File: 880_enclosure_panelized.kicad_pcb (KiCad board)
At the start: 2 copper layers, 351.5 x 39 mm, 182 parts, among them CON1 BARREL_JACK, J1 RUN/STOP, J10 RS IN, J11 CP IN, J12 MA IN, J13 CB IN, J14 CY IN, J15 OH IN, J16 CH IN, J17 IN 1, J18 IN 2, J19 IN 3, J2 SYNC24 CLK, J20 IN 4, J21 MULT IN, J22 SUM, J23 JACK_STEREO, J24 JACK_TRS_SWITCHED, J25 JACK_STEREO, J3 ASSIGN 1, J4 ASSIGN 2, J5 BD IN, J6 SD IN, J7 LT IN, J8 MT IN, J9 HT IN, P1 CONN_02X03, P10 CONN_01X02, P11 CONN_01X03, P2 CONN_01X02, P3 CONN_02X08, P4 CONN_01X03, P5 CONN_01X04, P6 CONN_01X04, P7 CONN_01X03, P8 CONN_01X03, P9 CONN_01X03, Q1 MMBT3904, Q10 MMBT3904, Q11 MMBT3904, Q12 MMBT3904, Q13 MMBT3904, Q14 C945, Q15 A733, Q2 MMBT3904, Q3 MMBT3904, Q4 MMBT3904, Q5 MMBT3904, Q6 MMBT3904, Q7 MMBT3904, Q8 MMBT3904, Q9 MMBT3904, SW1 SPST, U1 74HC165, U2 74HC165, U3 VX078-500, U4 VX078-500, U5 4558, U6 4558, X1 MIDI OUT, X2 SYNC24

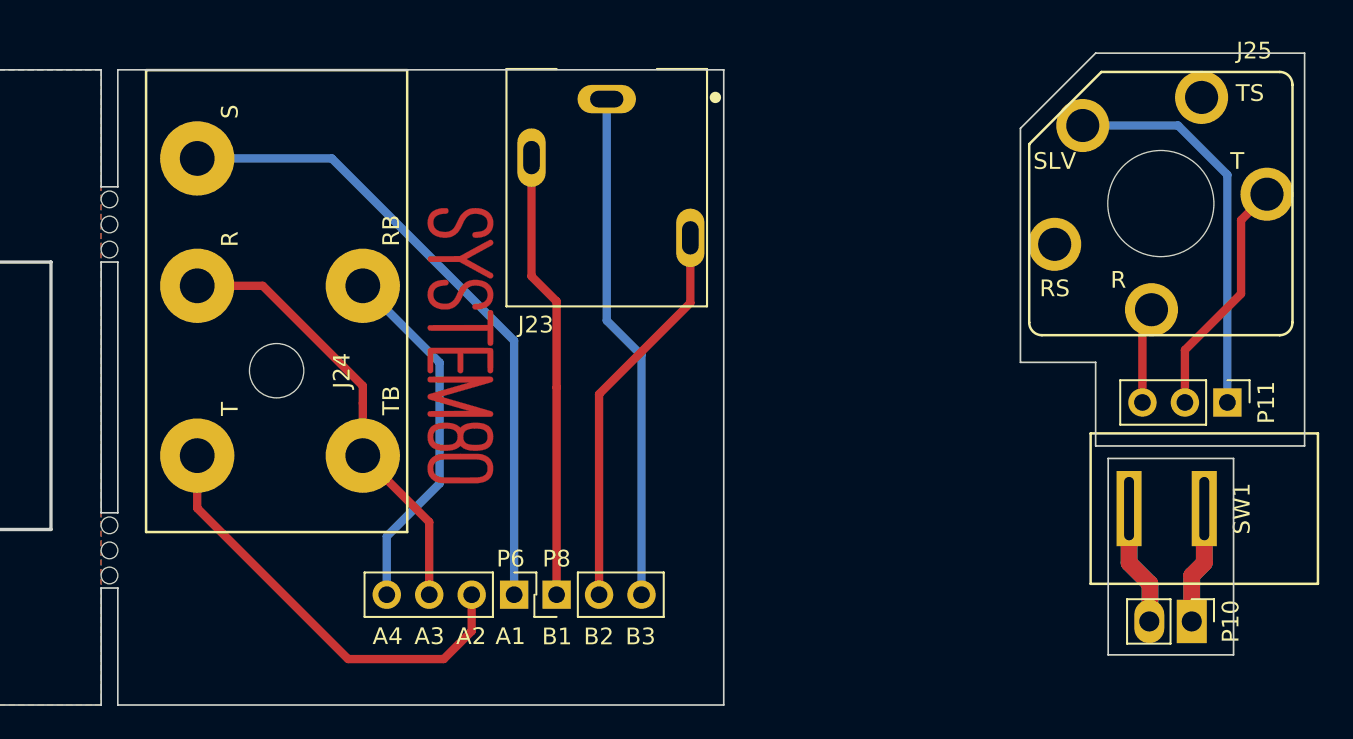
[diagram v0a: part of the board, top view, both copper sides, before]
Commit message: panelizing pcb
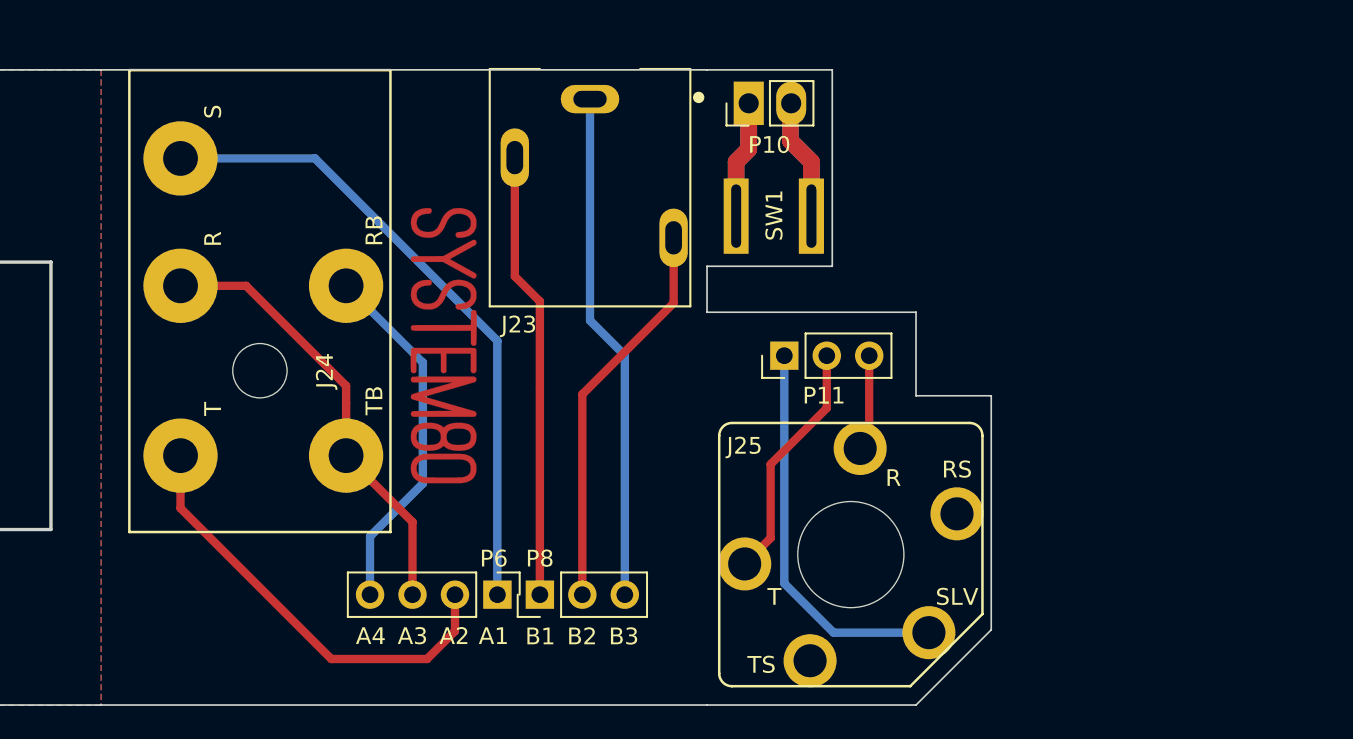
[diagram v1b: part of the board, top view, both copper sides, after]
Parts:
- removed HOLE-M3 (x6): VAL**, MyModules:HOLE-M3
- moved P10 40.8 mm to (330.2, 59.5), turned to 90 degrees
- moved SW1 33.0 mm to (329.5, 66.3), turned to 180 degrees
- moved J25 28.0 mm to (336.4, 86.5), turned to 0 degrees
- moved P11 26.7 mm to (332.4, 74.6), turned to 90 degrees
- moved G*** 1.00 mm to (312.0, 74.0)
- moved J23 1.00 mm to (320.8, 59.2)
- moved J24 1.00 mm to (301.0, 75.5)
- moved P6 1.00 mm to (315.2, 88.9)
- moved P8 1.00 mm to (317.8, 88.9)
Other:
- board size 351.5 x 39 mm -> 332.8 x 38 mm

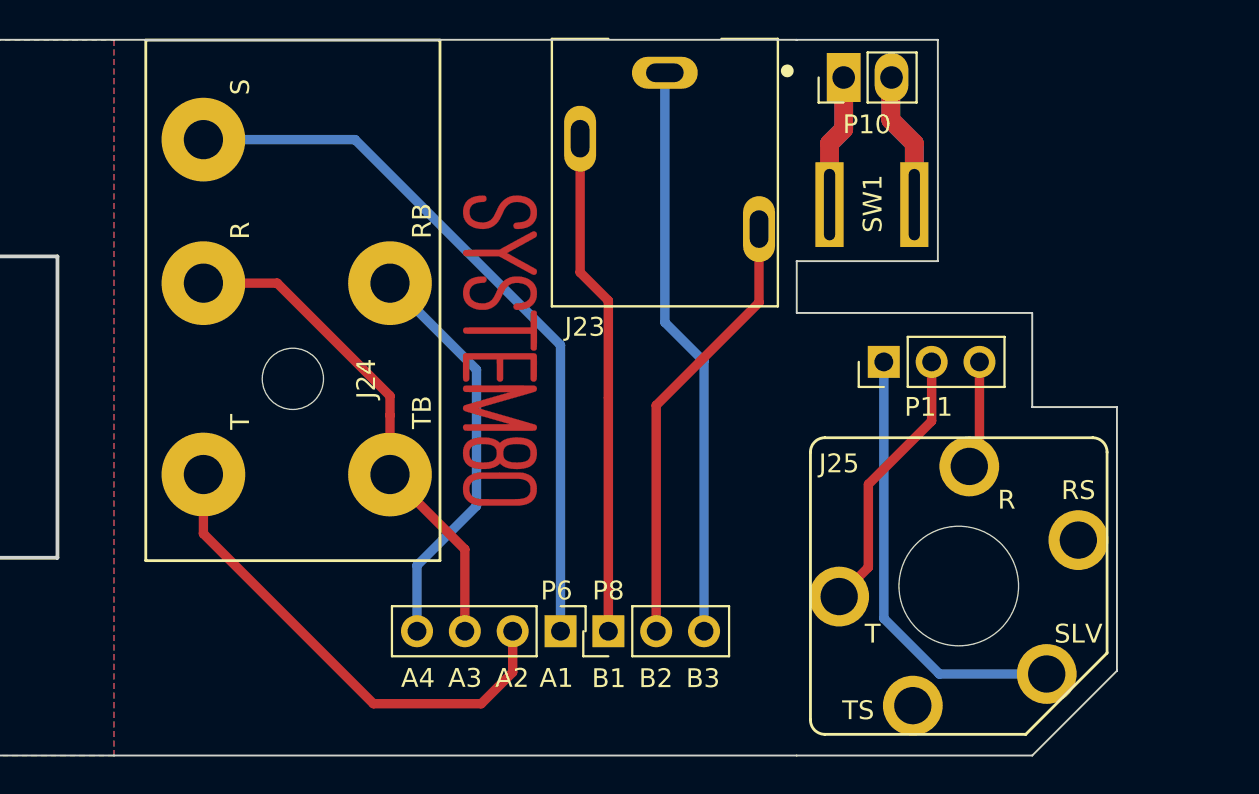
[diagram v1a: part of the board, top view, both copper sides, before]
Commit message: panelized sub-boards
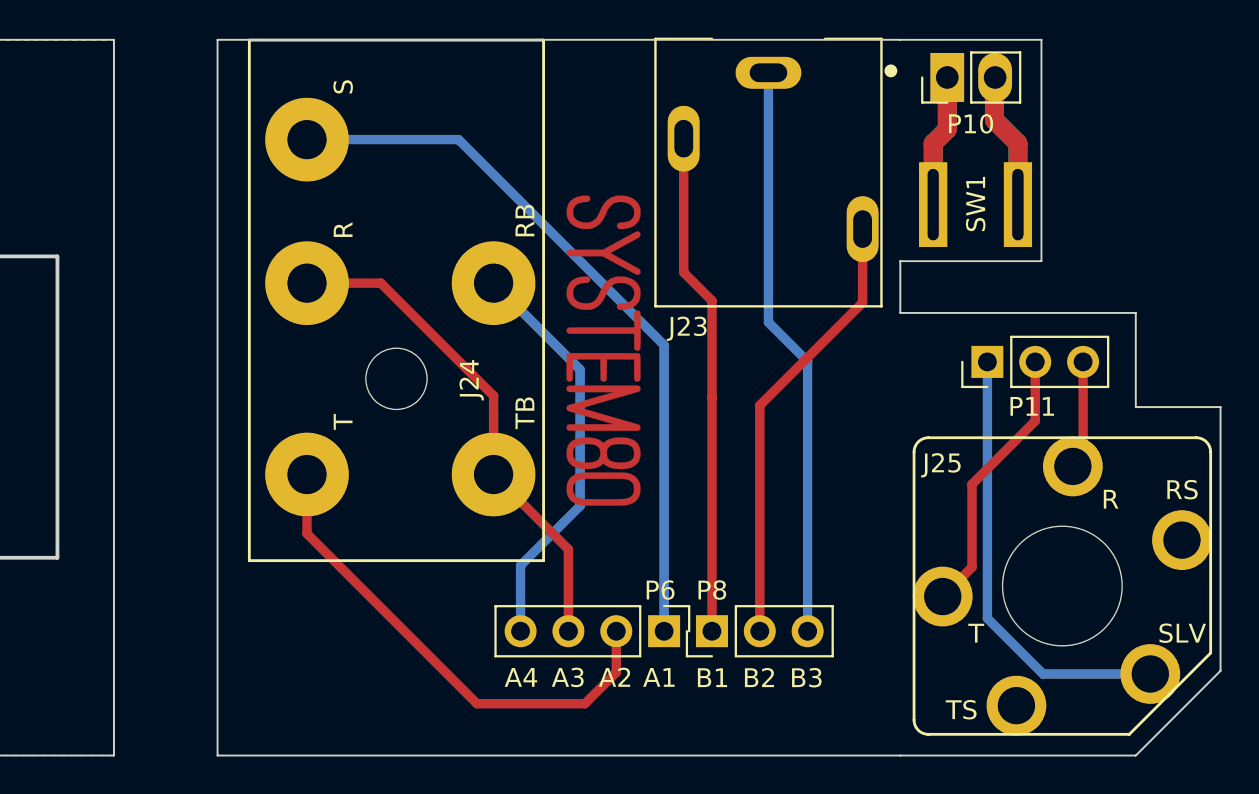
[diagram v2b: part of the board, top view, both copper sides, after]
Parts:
- moved G*** 5.50 mm to (317.5, 74.0)
- moved J23 5.50 mm to (326.2, 59.2)
- moved J24 5.50 mm to (306.5, 75.5)
- moved J25 5.50 mm to (341.9, 86.5)
- moved P10 5.50 mm to (335.7, 59.5)
- moved P11 5.50 mm to (337.9, 74.6)
- moved P6 5.50 mm to (320.7, 88.9)
- moved P8 5.50 mm to (323.2, 88.9)
- moved SW1 5.50 mm to (335.0, 66.3)
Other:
- board size 332.8 x 38 mm -> 338.3 x 38 mm

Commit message: v1.1 ordered plus sub boards
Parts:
- removed the G*** at (317.5, 74.0)
- removed J23: JACK_STEREO, MyModules:CUI_SJ1-3513
- removed J24: JACK_TRS_SWITCHED, MyModules:RA49B14B_SWITCHCRAFT
- removed J25: JACK_STEREO, MyModules:11XPC-SWITCH_CRAFT
- removed P10: CONN_01X02, Pin_Headers:Pin_Header_Straight_1x02_Pitch2.54mm
- removed P11, P8: CONN_01X03, Pin_Headers:Pin_Header_Straight_1x03_Pitch2.54mm
- removed P6: CONN_01X04, Pin_Headers:Pin_Header_Straight_1x04_Pitch2.54mm
- removed SW1: SPST, MyModules:PR_PPR_ROCKER_SW
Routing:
- net Net-(J24-Pad1): track 38.7 -> 0.00 mm
- net Net-(J23-Pad1): track 30.6 -> 0.00 mm
- net Net-(J23-Pad2): track 26.8 -> 0.00 mm
- net Net-(J24-Pad3): track 26.5 -> 0.00 mm
- net Net-(J24-Pad2): track 26.2 -> 0.00 mm
- net Net-(J23-Pad3): track 23.6 -> 0.00 mm
- net Net-(J25-Pad1): track 23.5 -> 0.00 mm
- net Net-(J24-Pad4): track 21.7 -> 0.00 mm
- net Net-(P10-Pad2): track 14.5 -> 0.00 mm
- net Net-(J25-Pad2): track 14.5 -> 0.00 mm
- net Net-(P10-Pad1): track 14.1 -> 0.00 mm
- net GND: track 88.3 -> 95.8 mm
- net Net-(J25-Pad3): track 5.77 -> 0.00 mm
- net Net-(J21-Pad2): track 29.6 -> 32.1 mm
- net -V: track 336.5 -> 335.7 mm
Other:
- board size 338.3 x 38 mm -> 279.5 x 38 mm
- board text added: "880ENC MAIN BOARD r1.1 6/2019"
- board text removed: "880 case board r1.1 6/2019"

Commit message: separating digital and audio gnd planes
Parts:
- removed G*** (x2): LOGO, LOGO
- removed P9: CONN_01X03, Pin_Headers:Pin_Header_Straight_1x03_Pitch2.54mm
- removed Q13: MMBT3904, MyModules:SOT23-132-JRL
- removed R44: 100K, MyModules:SM0603-R-YAGEO
- removed R45: 10K, MyModules:SM0603-R-YAGEO
- removed R53: 330K, MyModules:SM0603-R-YAGEO
- removed TP3: CONN_1, MyModules:TEST_POINT_LOOP_4592
- added C19: 0.1µ, MyModules:SM0603-C-MURATA, B.Cu at (120.5, 75.8)
- C15: value 33μ -> 1µ; footprint Capacitors_SMD:CP_Elec_5x5.3 -> Capacitors_SMD:C_0805
- D17: value D_Schottky -> MBRS240LT3G
- R42: value 10K -> 47K
- moved C15 110.6 mm to (122.2, 75.8), turned to 90 degrees
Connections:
- C1 pad 2: GND -> GNDD
- C15 pad 1: Net-(C15-Pad1) -> +5V
- C15 pad 2: Net-(C15-Pad2) -> GNDD
- C16 pad 2: Net-(C15-Pad2) -> Net-(C16-Pad2)
- C2 pad 2: GND -> GNDD
- C3 pad 2: GND -> GNDD
- D10 pad 2: GND -> GNDD
- D11 pad 2: GND -> GNDD
- D12 pad 2: GND -> GNDD
- D13 pad 2: GND -> GNDD
- D14 pad 2: GND -> GNDD
- D15 pad 2: GND -> GNDD
- D16 pad 2: GND -> GNDD
- D2 pad 2: GND -> GNDD
- D4 pad 2: GND -> GNDD
- D5 pad 2: GND -> GNDD
- D6 pad 2: GND -> GNDD
- D7 pad 2: GND -> GNDD
- D8 pad 2: GND -> GNDD
- D9 pad 2: GND -> GNDD
- ISP1 pad 5: ~RESET -> Net-(ISP1-Pad5)
- ISP1 pad 6: GND -> GNDD
- J1 pad 1: GND -> GNDD
- J10 pad 1: GND -> GNDD
- J10 pad 2: GND -> GNDD
- J11 pad 1: GND -> GNDD
- J11 pad 2: GND -> GNDD
- J12 pad 1: GND -> GNDD
- J12 pad 2: GND -> GNDD
- J13 pad 1: GND -> GNDD
- J13 pad 2: GND -> GNDD
- J14 pad 1: GND -> GNDD
- J14 pad 2: GND -> GNDD
- J15 pad 1: GND -> GNDD
- J15 pad 2: GND -> GNDD
- J16 pad 1: GND -> GNDD
- J16 pad 2: GND -> GNDD
- J2 pad 1: GND -> GNDD
- J3 pad 1: GND -> GNDD
- J4 pad 1: GND -> GNDD
- J5 pad 1: GND -> GNDD
- J5 pad 2: GND -> GNDD
- J6 pad 1: GND -> GNDD
- J6 pad 2: GND -> GNDD
- J7 pad 1: GND -> GNDD
- J7 pad 2: GND -> GNDD
- J8 pad 1: GND -> GNDD
- J8 pad 2: GND -> GNDD
- J9 pad 1: GND -> GNDD
- J9 pad 2: GND -> GNDD
- P1 pad 3: GND -> GNDD
- P7 pad 3: GND -> /PHONE_GND
- Q1 pad 2: GND -> GNDD
- Q10 pad 2: GND -> GNDD
- Q11 pad 2: GND -> GNDD
- Q12 pad 2: GND -> GNDD
- Q2 pad 2: GND -> GNDD
- Q3 pad 2: GND -> GNDD
- Q4 pad 2: GND -> GNDD
- Q5 pad 2: GND -> GNDD
- Q6 pad 2: GND -> GNDD
- Q7 pad 2: GND -> GNDD
- Q8 pad 2: GND -> GNDD
- Q9 pad 2: GND -> GNDD
- R10 pad 2: GND -> GNDD
- R11 pad 2: GND -> GNDD
- R12 pad 2: GND -> GNDD
- R13 pad 2: GND -> GNDD
- R2 pad 1: GND -> GNDD
- R22 pad 2: GND -> GNDD
- R23 pad 2: GND -> GNDD
- R24 pad 2: GND -> GNDD
- R25 pad 2: GND -> GNDD
- R34 pad 2: GND -> GNDD
- R35 pad 2: GND -> GNDD
- R36 pad 2: GND -> GNDD
- R37 pad 2: GND -> GNDD
- R42 pad 1: +5V -> DIN_RESET
- R42 pad 2: ~RESET -> GNDD
- R43 pad 1: ~RESET -> DIN_FILL
- R43 pad 2: Net-(Q13-Pad1) -> GNDD
- R51 pad 2: Net-(C15-Pad2) -> Net-(C16-Pad2)
- R52 pad 1: Net-(C15-Pad2) -> Net-(C16-Pad2)
- U1 pad 15: /~CE -> GNDD
- U1 pad 8: GND -> GNDD
- U2 pad 15: /~CE -> GNDD
- U2 pad 3: GND -> GNDD
- U2 pad 4: GND -> GNDD
- U2 pad 5: GND -> GNDD
- U2 pad 6: GND -> GNDD
- U2 pad 8: GND -> GNDD
- U5 pad 6: Net-(C15-Pad2) -> Net-(C16-Pad2)
- X1 pad 2: GND -> GNDD
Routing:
- net GND: track 95.8 -> 31.1 mm, vias 17 -> 12
- net /~CE: track 62.2 -> 0.00 mm, vias 2 -> 0
- net ~RESET: track 56.2 -> 0.00 mm, vias 2 -> 0
- net Net-(ISP1-Pad5): track 0.00 -> 29.0 mm
- net GNDD: track 0.00 -> 27.7 mm, vias 0 -> 5
- net DIN_FILL: track 11.4 -> 36.9 mm, vias 0 -> 2
- net Net-(C15-Pad2): track 11.0 -> 0.00 mm
- net Net-(P9-Pad3): track 7.31 -> 0.00 mm
- net Net-(C16-Pad2): track 0.00 -> 6.99 mm
- net Net-(C15-Pad1): track 3.81 -> 0.00 mm
- net Net-(Q13-Pad1): track 3.73 -> 0.00 mm
- net Net-(C16-Pad1): track 64.4 -> 61.7 mm
- net +5V: track 333.6 -> 335.3 mm
- net DIN_RESET: track 31.3 -> 32.9 mm
- added copper zone on B.Cu, net GNDD
- added copper zone on F.Cu, net GNDD
- removed copper zone on B.Cu, net GND
- removed copper zone on F.Cu, net GND
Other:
- board text added: "880ENC MAIN BOARD r1.2 9/2019"
- board text removed: "880ENC MAIN BOARD r1.1 6/2019"

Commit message: working on 4 layer, separate digital and audio gnd planes
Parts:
- added U7: 74HC1G125, Housings_SSOP:TSOP-5_1.65x3.05mm_Pitch0.95mm, B.Cu at (145.5, 86.5)
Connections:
- U2 pad 9: ISP_MISO -> Net-(U2-Pad9)
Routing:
- net DIN_RUN_STOP: track 27.9 -> 102.7 mm, vias 0 -> 1
- net -V: track 335.7 -> 289.2 mm
- net ISP_MISO: track 17.5 -> 27.4 mm, vias 0 -> 1
- net Net-(U2-Pad9): track 0.00 -> 9.74 mm
- net +5V: track 335.3 -> 342.6 mm, vias 17 -> 18
- net +V: track 305.5 -> 310.1 mm
- net GNDD: track 27.7 -> 29.5 mm, vias 5 -> 6
- added copper zone on F.Cu, net GND
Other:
- copper layers 2 -> 4
- board text removed: "RESET"
- board text removed: "~CE"

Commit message: routed
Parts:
- moved R43 72.7 mm to (87.0, 77.8), turned to 90 degrees
- moved R42 72.5 mm to (88.5, 68.0), turned to 270 degrees
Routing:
- net GNDD: track 29.5 -> 78.9 mm
- net Net-(ISP1-Pad5): track 29.0 -> 0.00 mm
- net DIN_FILL: track 36.9 -> 12.9 mm, vias 2 -> 0
- net -V: track 289.2 -> 295.3 mm
- net +5V: track 342.6 -> 338.0 mm, vias 18 -> 17
- net DIN_RESET: track 32.9 -> 31.7 mm
- net ISP_SCK: track 33.1 -> 32.3 mm
- net Net-(U1-Pad9): track 41.5 -> 40.9 mm
- net Net-(R1-Pad1): track 52.2 -> 51.6 mm
- added copper zone on B.Cu, net GND
- added copper zone on In2.Cu, net GNDD
